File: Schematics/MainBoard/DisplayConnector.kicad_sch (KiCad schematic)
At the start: 11 parts, among them J5 Conn_02x20_Odd_Even, U8 TXS0108, U9 TXS0108

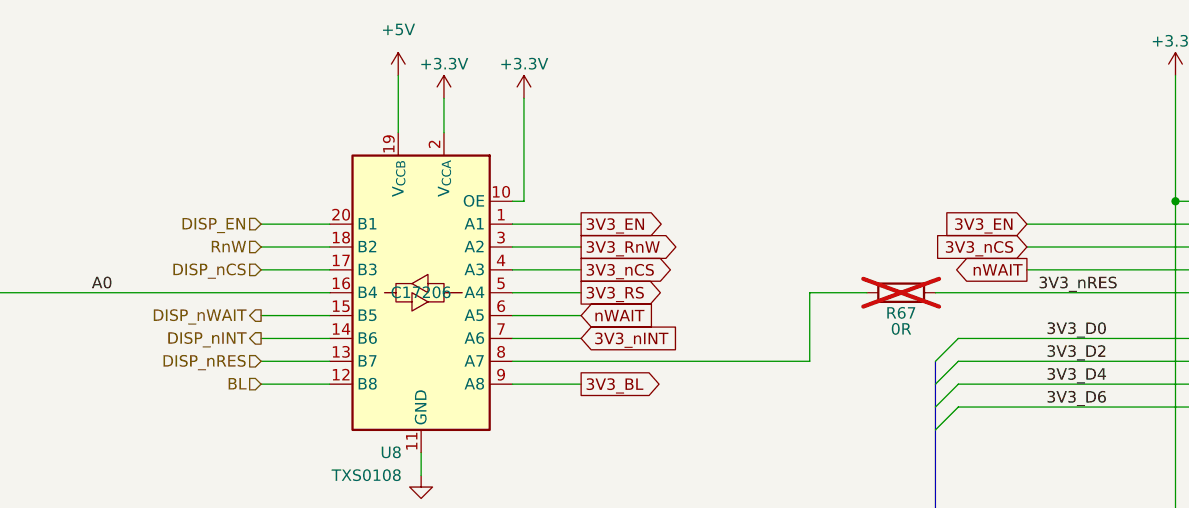
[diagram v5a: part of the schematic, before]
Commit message: Add some comments to schematic, update README, start on GLUE
Add some comments to schematic, update README, start on GLUE
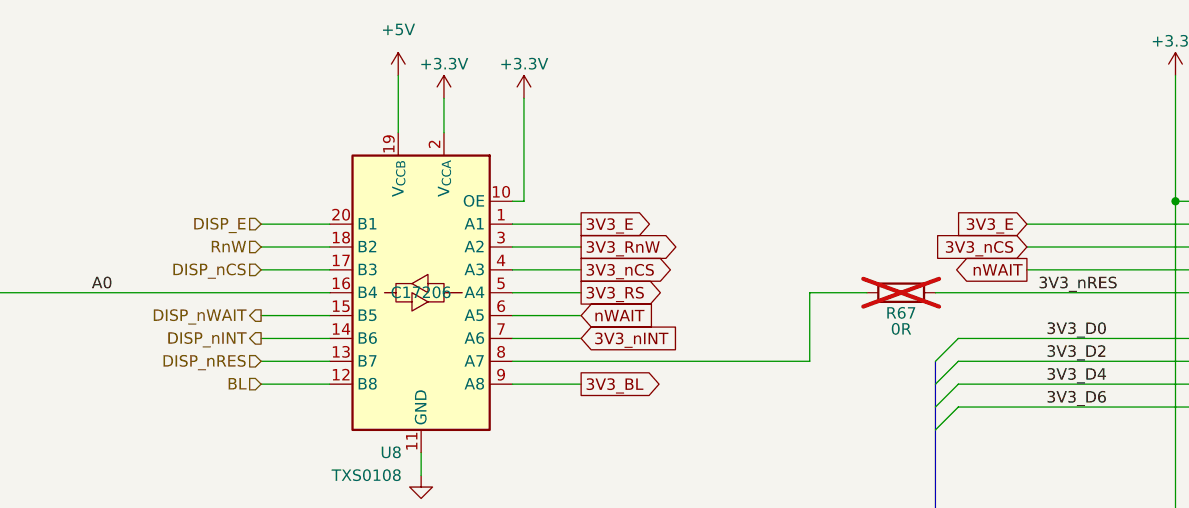
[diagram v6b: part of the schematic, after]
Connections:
- net 3V3_EN renamed 3V3_E
- net DISP_EN renamed DISP_E
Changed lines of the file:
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@@
 		)
 	)
-	(global_label "3V3_EN"
+	(global_label "3V3_E"
 		(shape input)
 		(at 165.1 53.34 180)
@@
 		)
 		(property "Intersheetrefs" "${INTERSHEET_REFS}"
-			(at 155.1601 53.34 0)
+			(at 156.4906 53.34 0)
 			(effects
 				(font
@@
 		)
 	)
-	(global_label "3V3_EN"
+	(global_label "3V3_E"
 		(shape output)
 		(at 115.57 53.34 0)
@@
 		)
 		(property "Intersheetrefs" "${INTERSHEET_REFS}"
-			(at 125.5099 53.34 0)
+			(at 124.1794 53.34 0)
 			(effects
 				(font
@@
 		)
 	)
-	(hierarchical_label "DISP_EN"
+	(hierarchical_label "DISP_E"
 		(shape input)
 		(at 80.01 53.34 180)
@@
 		)
 		(instances
-			(project "LT6502"
+			(project "MainBoard"
 				(path "/a2243a34-697c-4939-97f7-df548e421864/825e1c9a-e371-499a-ad28-43b57b6b2827"
 					(reference "#PWR0149")
@@
 		)
 		(instances
-			(project "LT6502"
+			(project "MainBoard"
 				(path "/a2243a34-697c-4939-97f7-df548e421864/825e1c9a-e371-499a-ad28-43b57b6b2827"
 					(reference "#PWR0151")
@@
 		)
 		(instances
-			(project "LT6502"
+			(project "MainBoard"
 				(path "/a2243a34-697c-4939-97f7-df548e421864/825e1c9a-e371-499a-ad28-43b57b6b2827"
 					(reference "#PWR0237")
@@
 		)
 		(instances
-			(project "LT6502"
+			(project "MainBoard"
 				(path "/a2243a34-697c-4939-97f7-df548e421864/825e1c9a-e371-499a-ad28-43b57b6b2827"
 					(reference "R67")
@@
 		)
 		(instances
-			(project "LT6502"
+			(project "MainBoard"
 				(path "/a2243a34-697c-4939-97f7-df548e421864/825e1c9a-e371-499a-ad28-43b57b6b2827"
 					(reference "C36")
@@
 		)
 		(instances
-			(project "LT6502"
+			(project "MainBoard"
 				(path "/a2243a34-697c-4939-97f7-df548e421864/825e1c9a-e371-499a-ad28-43b57b6b2827"
 					(reference "#PWR0141")
@@
 		)
 		(instances
-			(project "LT6502"
+			(project "MainBoard"
 				(path "/a2243a34-697c-4939-97f7-df548e421864/825e1c9a-e371-499a-ad28-43b57b6b2827"
 					(reference "#PWR0137")
@@
 		)
 		(instances
-			(project "LT6502"
+			(project "MainBoard"
 				(path "/a2243a34-697c-4939-97f7-df548e421864/825e1c9a-e371-499a-ad28-43b57b6b2827"
 					(reference "#PWR0150")
@@
 		)
 		(instances
-			(project "LT6502"
+			(project "MainBoard"
 				(path "/a2243a34-697c-4939-97f7-df548e421864/825e1c9a-e371-499a-ad28-43b57b6b2827"
 					(reference "#PWR0142")
@@
 		)
 		(instances
-			(project ""
+			(project "MainBoard"
 				(path "/a2243a34-697c-4939-97f7-df548e421864/825e1c9a-e371-499a-ad28-43b57b6b2827"
 					(reference "J5")
@@
 		)
 		(instances
-			(project "LT6502"
+			(project "MainBoard"
 				(path "/a2243a34-697c-4939-97f7-df548e421864/825e1c9a-e371-499a-ad28-43b57b6b2827"
 					(reference "C35")
@@
 		)
 		(instances
-			(project "LT6502"
+			(project "MainBoard"
 				(path "/a2243a34-697c-4939-97f7-df548e421864/825e1c9a-e371-499a-ad28-43b57b6b2827"
 					(reference "U9")
@@
 		)
 		(instances
-			(project "LT6502"
+			(project "MainBoard"
 				(path "/a2243a34-697c-4939-97f7-df548e421864/825e1c9a-e371-499a-ad28-43b57b6b2827"
 					(reference "#PWR0144")
@@
 		)
 		(instances
-			(project "LT6502"
+			(project "MainBoard"
 				(path "/a2243a34-697c-4939-97f7-df548e421864/825e1c9a-e371-499a-ad28-43b57b6b2827"
 					(reference "#PWR0146")
@@
 		)
 		(instances
-			(project "LT6502"
+			(project "MainBoard"
 				(path "/a2243a34-697c-4939-97f7-df548e421864/825e1c9a-e371-499a-ad28-43b57b6b2827"
 					(reference "#PWR0136")
@@
 		)
 		(instances
-			(project "LT6502"
+			(project "MainBoard"
 				(path "/a2243a34-697c-4939-97f7-df548e421864/825e1c9a-e371-499a-ad28-43b57b6b2827"
 					(reference "U8")
@@
 		)
 		(instances
-			(project "LT6502"
+			(project "MainBoard"
 				(path "/a2243a34-697c-4939-97f7-df548e421864/825e1c9a-e371-499a-ad28-43b57b6b2827"
 					(reference "#PWR0225")
@@
 		)
 		(instances
-			(project "LT6502"
+			(project "MainBoard"
 				(path "/a2243a34-697c-4939-97f7-df548e421864/825e1c9a-e371-499a-ad28-43b57b6b2827"
 					(reference "#PWR0148")
@@
 		)
 		(instances
-			(project "LT6502"
+			(project "MainBoard"
 				(path "/a2243a34-697c-4939-97f7-df548e421864/825e1c9a-e371-499a-ad28-43b57b6b2827"
 					(reference "#PWR0140")
@@
 		)
 		(instances
-			(project "LT6502"
+			(project "MainBoard"
 				(path "/a2243a34-697c-4939-97f7-df548e421864/825e1c9a-e371-499a-ad28-43b57b6b2827"
 					(reference "C52")
@@
 		)
 		(instances
-			(project "LT6502"
+			(project "MainBoard"
 				(path "/a2243a34-697c-4939-97f7-df548e421864/825e1c9a-e371-499a-ad28-43b57b6b2827"
 					(reference "R91")
@@
 		)
 		(instances
-			(project "LT6502"
+			(project "MainBoard"
 				(path "/a2243a34-697c-4939-97f7-df548e421864/825e1c9a-e371-499a-ad28-43b57b6b2827"
 					(reference "R92")
@@
 		)
 		(instances
-			(project "LT6502"
+			(project "MainBoard"
 				(path "/a2243a34-697c-4939-97f7-df548e421864/825e1c9a-e371-499a-ad28-43b57b6b2827"
 					(reference "R68")
@@
 		)
 		(instances
-			(project "LT6502"
+			(project "MainBoard"
 				(path "/a2243a34-697c-4939-97f7-df548e421864/825e1c9a-e371-499a-ad28-43b57b6b2827"
 					(reference "#PWR0139")
@@
 		)
 		(instances
-			(project "LT6502"
+			(project "MainBoard"
 				(path "/a2243a34-697c-4939-97f7-df548e421864/825e1c9a-e371-499a-ad28-43b57b6b2827"
 					(reference "#PWR0145")
@@
 		)
 		(instances
-			(project "LT6502"
+			(project "MainBoard"
 				(path "/a2243a34-697c-4939-97f7-df548e421864/825e1c9a-e371-499a-ad28-43b57b6b2827"
 					(reference "C51")
@@
 		)
 		(instances
-			(project "LT6502"
+			(project "MainBoard"
 				(path "/a2243a34-697c-4939-97f7-df548e421864/825e1c9a-e371-499a-ad28-43b57b6b2827"
 					(reference "#PWR0227")
@@
 		)
 		(instances
-			(project "LT6502"
+			(project "MainBoard"
 				(path "/a2243a34-697c-4939-97f7-df548e421864/825e1c9a-e371-499a-ad28-43b57b6b2827"
 					(reference "#PWR0143")
@@
 		)
 		(instances
-			(project "LT6502"
+			(project "MainBoard"
 				(path "/a2243a34-697c-4939-97f7-df548e421864/825e1c9a-e371-499a-ad28-43b57b6b2827"
 					(reference "#PWR0138")
@@
 		)
 		(instances
-			(project "LT6502"
+			(project "MainBoard"
 				(path "/a2243a34-697c-4939-97f7-df548e421864/825e1c9a-e371-499a-ad28-43b57b6b2827"
 					(reference "#PWR0226")
@@
 		)
 		(instances
-			(project "LT6502"
+			(project "MainBoard"
 				(path "/a2243a34-697c-4939-97f7-df548e421864/825e1c9a-e371-499a-ad28-43b57b6b2827"
 					(reference "#PWR0224")
